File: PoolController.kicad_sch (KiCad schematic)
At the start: 19 parts, among them J1 RJ12, J2 RJ12, J3 Header, J4 Conn_02x12_Counter_Clockwise, Q1 MMBT3904, U1 LM2678S-5.0/NOPB

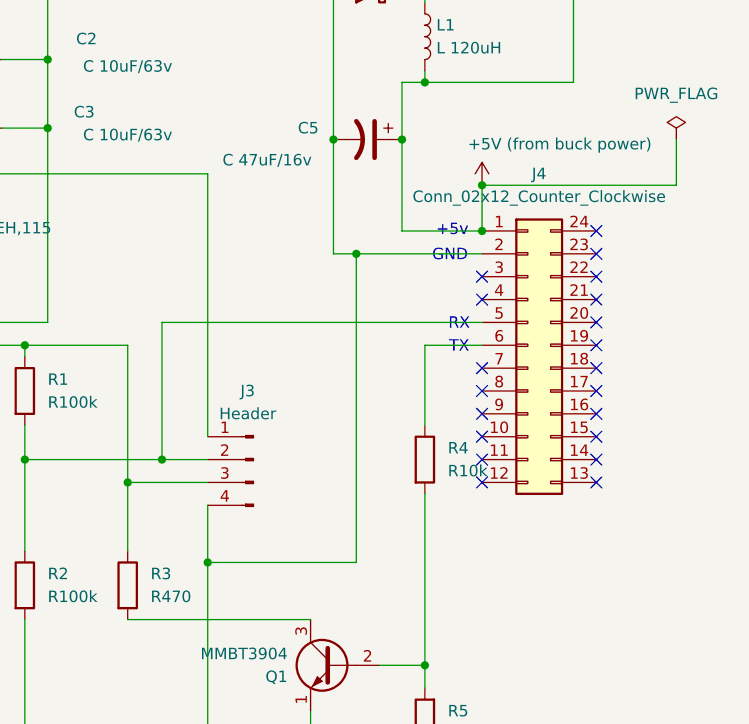
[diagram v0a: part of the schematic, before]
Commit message: ### Changed - Rev 11 - changed RJ12 connectors to 5324 6P6C pieces and updated pcb - Rev 11 - additional gnd connecting vias under buck (U1)
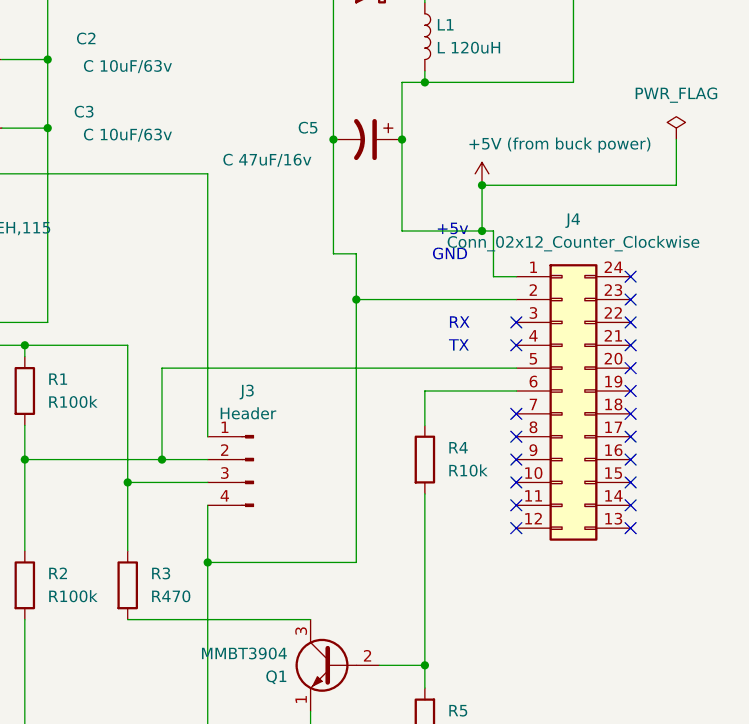
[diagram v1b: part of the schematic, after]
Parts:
- J1, J2: footprint Connector_RJ:RJ25_Wayconn_MJEA-660X1_Horizontal -> Connector_RJ:RJ25_RJ12_5324_mini; MPN MJEA-660X1XXX -> (none); Manufacturer Wayconn -> (none)
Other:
- moved on the sheet: J4
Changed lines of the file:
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@@
 	(title_block
 		(title "Connect 10 Controller")
-		(date "2026-02-18")
-		(rev "10")
+		(date "2026-02-24")
+		(rev "11")
 	)
 	(text "+5v"
@@
 	)
 	(junction
-		(at 130.81 86.36)
-		(diameter 0)
-		(color 0 0 0 0)
-	)
-	(junction
 		(at 144.78 83.82)
 		(diameter 0)
@@
 	)
 	(junction
+		(at 130.81 91.44)
+		(diameter 0)
+		(color 0 0 0 0)
+	)
+	(junction
 		(at 77.47 77.47)
 		(diameter 0)
@@
 	)
 	(no_connect
-		(at 157.48 96.52)
+		(at 161.29 101.6)
 	)
 	(no_connect
-		(at 144.78 99.06)
+		(at 148.59 104.14)
 	)
 	(no_connect
-		(at 157.48 106.68)
+		(at 161.29 111.76)
 	)
 	(no_connect
@@
 	)
 	(no_connect
-		(at 144.78 91.44)
+		(at 148.59 96.52)
 	)
 	(no_connect
-		(at 144.78 101.6)
+		(at 148.59 106.68)
 	)
 	(no_connect
-		(at 157.48 111.76)
+		(at 161.29 116.84)
 	)
 	(no_connect
-		(at 157.48 83.82)
+		(at 161.29 88.9)
 	)
 	(no_connect
-		(at 144.78 88.9)
+		(at 148.59 93.98)
 	)
 	(no_connect
-		(at 157.48 88.9)
+		(at 161.29 93.98)
 	)
 	(no_connect
-		(at 157.48 109.22)
+		(at 161.29 114.3)
 	)
 	(no_connect
@@
 	)
 	(no_connect
-		(at 157.48 93.98)
+		(at 161.29 99.06)
 	)
 	(no_connect
-		(at 157.48 104.14)
+		(at 161.29 109.22)
 	)
 	(no_connect
-		(at 157.48 99.06)
+		(at 161.29 104.14)
 	)
 	(no_connect
-		(at 144.78 106.68)
+		(at 148.59 111.76)
 	)
 	(no_connect
-		(at 157.48 91.44)
+		(at 161.29 96.52)
 	)
 	(no_connect
-		(at 157.48 101.6)
+		(at 161.29 106.68)
 	)
 	(no_connect
-		(at 157.48 86.36)
+		(at 161.29 91.44)
 	)
 	(no_connect
-		(at 144.78 109.22)
+		(at 148.59 114.3)
 	)
 	(no_connect
-		(at 144.78 104.14)
+		(at 148.59 109.22)
 	)
 	(no_connect
-		(at 144.78 111.76)
+		(at 148.59 116.84)
+	)
+	(wire
+		(pts
+			(xy 146.05 88.9) (xy 146.05 83.82)
+		)
+		(stroke
+			(width 0)
+			(type default)
+		)
 	)
 	(wire
@@
 	(wire
 		(pts
-			(xy 130.81 120.65) (xy 130.81 86.36)
+			(xy 130.81 120.65) (xy 130.81 91.44)
 		)
 		(stroke
@@
 	(wire
 		(pts
-			(xy 109.22 109.22) (xy 109.22 93.98)
+			(xy 109.22 109.22) (xy 109.22 99.06)
 		)
 		(stroke
@@
 	(wire
 		(pts
+			(xy 146.05 83.82) (xy 144.78 83.82)
+		)
+		(stroke
+			(width 0)
+			(type default)
+		)
+	)
+	(wire
+		(pts
 			(xy 52.07 152.4) (xy 55.88 152.4)
 		)
@@
 	(wire
 		(pts
-			(xy 144.78 96.52) (xy 138.43 96.52)
+			(xy 148.59 101.6) (xy 138.43 101.6)
 		)
 		(stroke
@@
 	(wire
 		(pts
-			(xy 138.43 96.52) (xy 138.43 105.41)
+			(xy 138.43 101.6) (xy 138.43 105.41)
 		)
 		(stroke
@@
 	(wire
 		(pts
-			(xy 109.22 93.98) (xy 144.78 93.98)
+			(xy 109.22 99.06) (xy 148.59 99.06)
+		)
+		(stroke
+			(width 0)
+			(type default)
+		)
+	)
+	(wire
+		(pts
+			(xy 130.81 91.44) (xy 130.81 86.36)
 		)
 		(stroke
@@
 	(wire
 		(pts
-			(xy 130.81 86.36) (xy 144.78 86.36)
+			(xy 130.81 91.44) (xy 148.59 91.44)
 		)
 		(stroke
@@
 	(wire
 		(pts
+			(xy 148.59 88.9) (xy 146.05 88.9)
+		)
+		(stroke
+			(width 0)
+			(type default)
+		)
+	)
+	(wire
+		(pts
 			(xy 58.42 83.82) (xy 58.42 91.44)
 		)
@@
 	(symbol
 		(lib_id "Connector_Generic:Conn_02x12_Counter_Clockwise")
-		(at 149.86 96.52 0)
+		(at 153.67 101.6 0)
 		(unit 1)
 		(exclude_from_sim no)
@@
 		(fields_autoplaced yes)
 		(property "Reference" "J4"
-			(at 151.13 77.47 0)
+			(at 154.94 82.55 0)
 			(effects
 				(font
@@
 		)
 		(property "Value" "Conn_02x12_Counter_Clockwise"
-			(at 151.13 80.01 0)
+			(at 154.94 85.09 0)
 			(effects
 				(font
@@
 		)
 		(property "Footprint" "Package_DIP:DIP-24_18.0mmx34.29mm_W15.24mm_Socket"
-			(at 149.86 96.52 0)
+			(at 153.67 101.6 0)
 			(effects
 				(font
@@
 		)
 		(property "Datasheet" "~"
-			(at 149.86 96.52 0)
+			(at 153.67 101.6 0)
 			(effects
 				(font
@@
 		)
 		(property "Description" "Generic connector, double row, 02x12, counter clockwise pin numbering scheme (similar to DIP package numbering), script generated (kicad-library-utils/schlib/autogen/connector/)"
-			(at 149.86 96.52 0)
+			(at 153.67 101.6 0)
 			(effects
 				(font
@@
 		)
 		(property "Manufacturer" "Amphenol ICC (FCI)"
-			(at 149.86 96.52 0)
+			(at 153.67 101.6 0)
 			(effects
 				(font
@@
 		)
 		(property "MPN" "DILB24P-223TLF"
-			(at 149.86 96.52 0)
+			(at 153.67 101.6 0)
 			(effects
 				(font
@@
 			)
 		)
-		(property "Footprint" "Connector_RJ:RJ25_Wayconn_MJEA-660X1_Horizontal"
+		(property "Footprint" "Connector_RJ:RJ25_RJ12_5324_mini"
 			(at 48.26 130.175 90)
 			(effects
@@
 			)
 		)
-		(property "Datasheet" "https://www.wayconn.com/rj25-6p6c-pcb-mount-ra/"
+		(property "Datasheet" "https://www.aliexpress.com/i/1005008617248283.html"
 			(at 48.26 130.175 90)
 			(effects
@@
 			)
 		)
-		(property "Manufacturer" "Wayconn"
+		(property "Manufacturer" ""
 			(at 48.26 130.81 0)
 			(effects
@@
 			)
 		)
-		(property "MPN" "MJEA-660X1XXX"
+		(property "MPN" ""
 			(at 48.26 130.81 0)
 			(effects
@@
 			)
 		)
-		(property "Footprint" "Connector_RJ:RJ25_Wayconn_MJEA-660X1_Horizontal"
+		(property "Footprint" "Connector_RJ:RJ25_RJ12_5324_mini"
 			(at 48.26 98.425 90)
 			(effects
@@
 			)
 		)
-		(property "Datasheet" "https://www.wayconn.com/rj25-6p6c-pcb-mount-ra/"
+		(property "Datasheet" "https://www.aliexpress.com/i/1005008617248283.html"
 			(at 48.26 98.425 90)
 			(effects
@@
 			)
 		)
-		(property "Manufacturer" "Wayconn"
+		(property "Manufacturer" ""
 			(at 48.26 99.06 0)
 			(effects
@@
 			)
 		)
-		(property "MPN" "MJEA-660X1XXX "
+		(property "MPN" ""
 			(at 48.26 99.06 0)
 			(effects

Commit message: Version 1.0.0 - Rev 13 of board.
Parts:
- Q1: footprint Package_TO_SOT_SMD:SOT-23 -> MMBT3904:SOT-23_MCC
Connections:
- net GND (from connector): now also Q1.2 (E); no longer Q1.1 (E)
- net at R4.2, R5.2: now also Q1.1 (B); no longer Q1.2 (B)
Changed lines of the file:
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@@
 	(title_block
 		(title "Connect 10 Controller")
-		(date "2026-02-24")
-		(rev "11")
+		(date "2026-04-01")
+		(rev "13")
 	)
 	(text "+5v"
@@
 			)
 		)
-		(property "Footprint" "Package_TO_SOT_SMD:SOT-23"
+		(property "Footprint" "MMBT3904:SOT-23_MCC"
 			(at 123.19 133.985 0)
 			(effects
@@
 				)
 				(justify left)
-				(hide yes)
-			)
-		)
+			)
+		)
